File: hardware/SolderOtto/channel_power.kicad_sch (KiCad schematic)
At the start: 16 parts, among them Q801 Q_Dual_NMOS, Q802 Q_Dual_NMOS, Q803 DTD123EK, Q804 DTD123EK, Q805 Q_Dual_NMOS, Q806 Q_Dual_NMOS, Q807 DTD123EK, Q808 DTD123EK, U801 VOM1271, U802 VOM1271, U803 VOM1271, U804 VOM1271

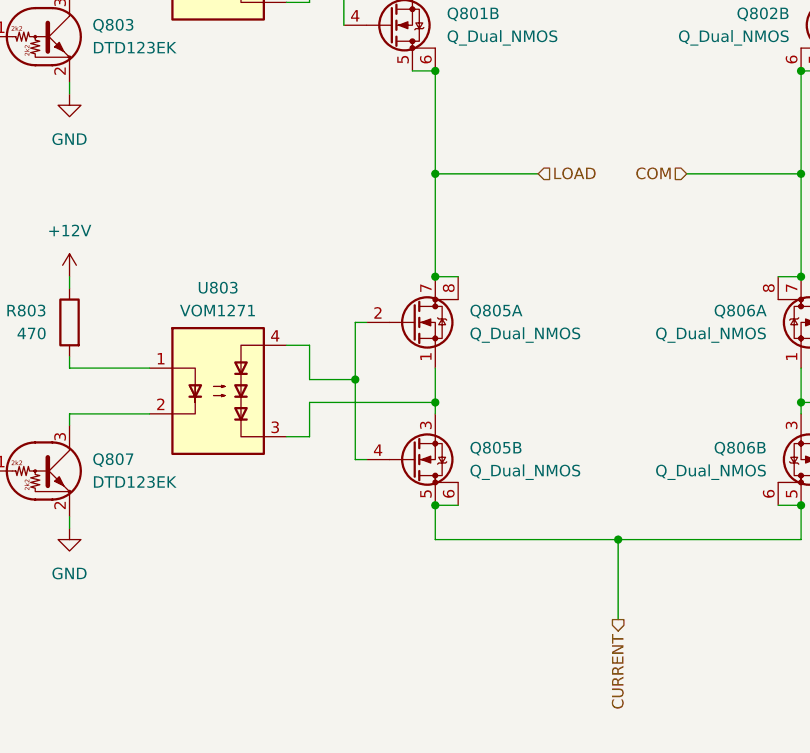
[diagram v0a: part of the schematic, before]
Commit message: add support for tweezers AM-120
change mcu to stm32h573VI
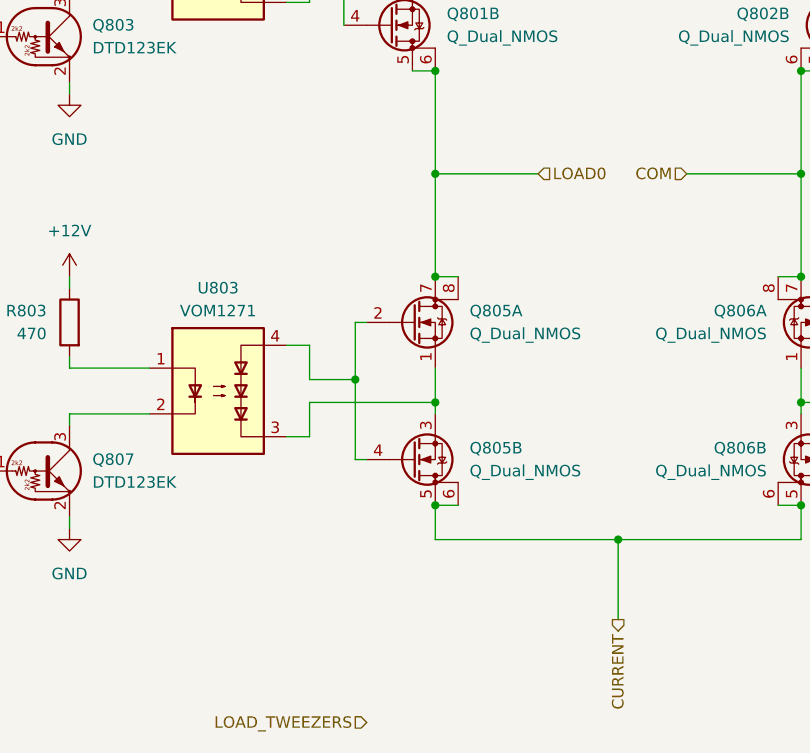
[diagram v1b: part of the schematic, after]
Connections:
- net LOAD renamed LOAD0
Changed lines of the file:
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@@
 		)
 	)
-	(hierarchical_label "LOAD"
+	(hierarchical_label "LOAD0"
 		(shape input)
 		(at 133.35 66.04 0)
@@
 			)
 			(justify right)
+		)
+	)
+	(hierarchical_label "LOAD_TWEEZERS"
+		(shape input)
+		(at 114.3 127 180)
+		(fields_autoplaced yes)
+		(effects
+			(font
+				(size 1.27 1.27)
+			)
+			(justify right)

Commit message: wip
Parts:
- added Q901: Q_Dual_NMOS, Package_SO:SO-8_3.9x4.9mm_P1.27mm, symbol Device:Q_Dual_NMOS_S1G1S2G2D2D2D1D1
- added Q902: DTD123EK, Package_TO_SOT_SMD:SC-59, symbol Transistor_BJT:DTD123E
- added R901: 470, Resistor_SMD:R_0603_1608Metric, symbol Device:R
- added U901: VOM1271, mylib_ic:SOP-4_3.8x4.1mm_P2.54mm, symbol mylib_diodes:VOM1271
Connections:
- net +12V: now also R901.1
- net 24V_{AC}: now also Q901.7 (D), Q901.8 (D)
- net GND: now also Q902.2 (E)
- net LOAD_SW_HIGH renamed LOAD0_SW_HIGH
- new net: Q901.1 (S), Q901.3 (S), U901.3
- new net: Q901.2 (G), Q901.4 (G), U901.4
- new net: Q902.3 (C), U901.2
- new net: R901.2, U901.1
- new net LOAD1: Q901.5 (D), Q901.6 (D)
- new net LOAD1_SW_HIGH: Q902.1 (B)
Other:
- moved on the sheet: Q801A, Q801B, Q802A, Q802B, Q803, Q804, Q805A, Q805B, Q806A, Q806B, Q807, Q808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

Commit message: create adapter to enclosure for display
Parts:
- renumbered Q801 to Q901, Q802 to Q902, Q901 to Q903, Q803 to Q904, Q804 to Q905, Q902 to Q906, Q805 to Q907, Q806 to Q908, Q807 to Q909, Q808 to Q910, R801 to R901, R802 to R902, R901 to R903, R803 to R904, R804 to R905, U801 to U901, U802 to U902, U901 to U903, U803 to U904, U804 to U905

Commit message: save work
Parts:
- renumbered Q901 to Q801, Q902 to Q802, Q903 to Q803, Q904 to Q804, Q905 to Q805, Q906 to Q806, Q907 to Q807, Q908 to Q808, Q909 to Q809, Q910 to Q810, R901 to R801, R902 to R802, R903 to R803, R904 to R804, R905 to R805, U901 to U801, U902 to U802, U903 to U803, U904 to U804, U905 to U805

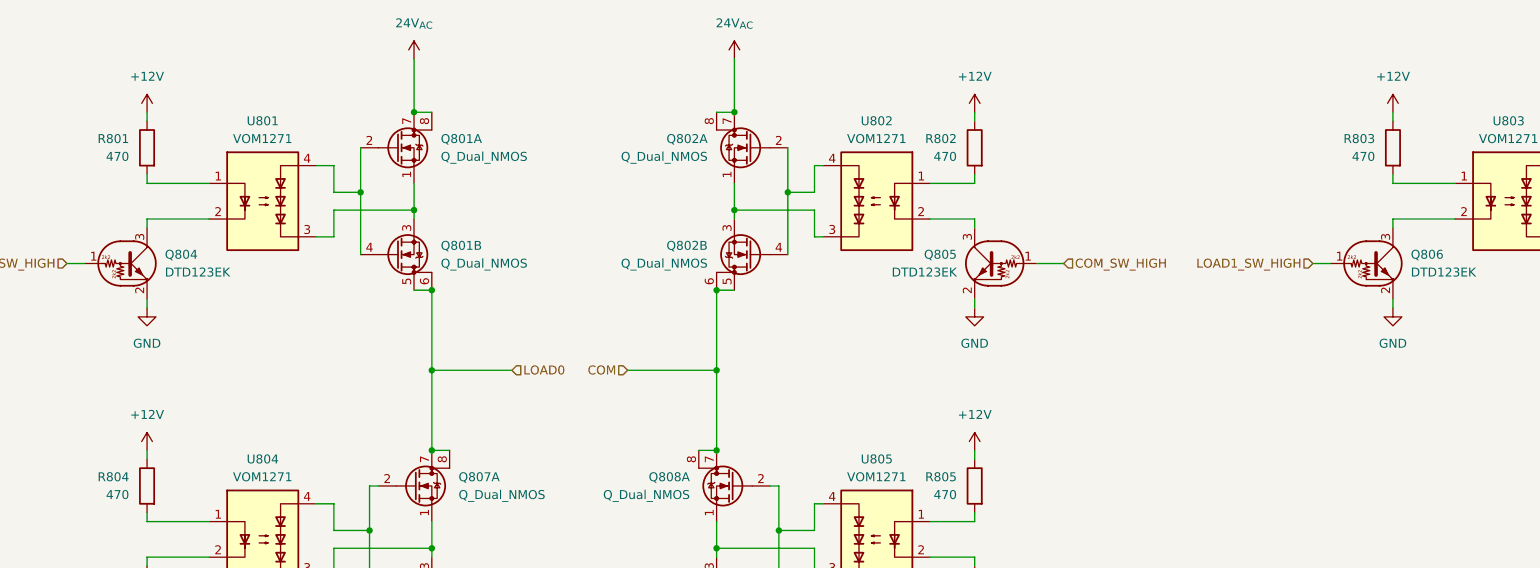
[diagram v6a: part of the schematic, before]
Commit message: remove 12V rail
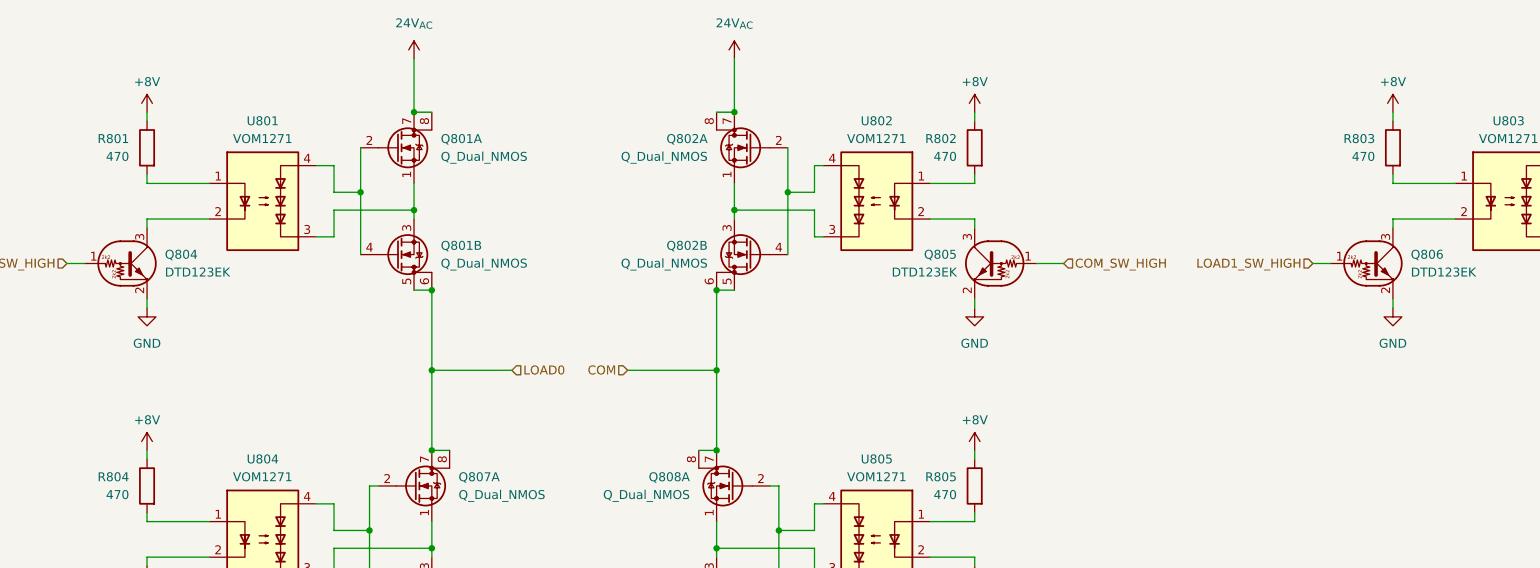
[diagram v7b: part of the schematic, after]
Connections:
- net +12V renamed +8V
